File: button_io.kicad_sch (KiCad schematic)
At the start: 0 parts

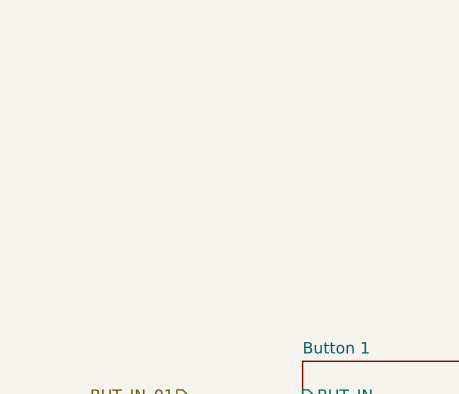
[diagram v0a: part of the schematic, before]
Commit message: Labeled expansion port, fixed en pin U19 (high)
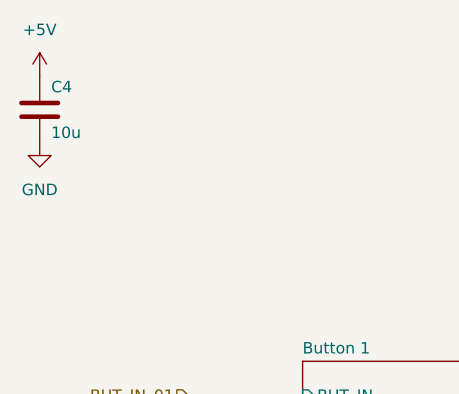
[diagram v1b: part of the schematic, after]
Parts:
- added C4: 10u, Capacitor_SMD:C_0805_2012Metric, symbol Device:C
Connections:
- new net +5V: C4.1
- new net GND: C4.2
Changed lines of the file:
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@@
+		)
+	)
+	(symbol
+		(lib_id "power:+5V")
+		(at 39.37 22.86 0)
+		(unit 1)
+		(exclude_from_sim no)
+		(in_bom yes)
+		(on_board yes)
+		(dnp no)
+		(fields_autoplaced yes)
+		(property "Reference" "#PWR052"
+			(at 39.37 26.67 0)
+			(effects
+				(font
+					(size 1.27 1.27)
+				)
+				(hide yes)
+			)
+		)
+		(property "Value" "+5V"
+			(at 39.37 17.78 0)
+			(effects
+				(font
+					(size 1.27 1.27)
+				)
+			)
+		)
+		(property "Footprint" ""
+			(at 39.37 22.86 0)
+			(effects
+				(font
+					(size 1.27 1.27)
+				)
+				(hide yes)
+			)
+		)
+		(property "Datasheet" ""
+			(at 39.37 22.86 0)
+			(effects
+				(font
+					(size 1.27 1.27)
+				)
+				(hide yes)
+			)
+		)
+		(property "Description" "Power symbol creates a global label with name \"+5V\""
+			(at 39.37 22.86 0)
+			(effects
+				(font
+					(size 1.27 1.27)
+				)
+				(hide yes)
+			)
+		)
+		(pin "1"
+		)
+		(instances
+			(project ""
+				(path "/4ab90003-ea4c-4878-8117-f834ac24f8d9/2279bf67-9a91-44f0-b5c7-36e7b6560aca"
+					(reference "#PWR052")
+					(unit 1)
+				)
+			)
+		)
+	)
+	(symbol
+		(lib_id "Device:C")
+		(at 39.37 26.67 0)
+		(unit 1)
+		(exclude_from_sim no)
+		(in_bom yes)
+		(on_board yes)
+		(dnp no)
+		(property "Reference" "C4"
+			(at 40.64 24.13 0)
+			(effects
+				(font
+					(size 1.27 1.27)
+				)
+				(justify left)
+			)
+		)
+		(property "Value" "10u"
+			(at 40.64 29.21 0)
+			(effects
+				(font
+					(size 1.27 1.27)
+				)
+				(justify left)
+			)
+		)
+		(property "Footprint" "Capacitor_SMD:C_0805_2012Metric"
+			(at 40.3352 30.48 0)
+			(effects
+				(font
+					(size 1.27 1.27)
+				)
+				(hide yes)
+			)
+		)
+		(property "Datasheet" "https://www.lcsc.com/product-detail/Multilayer-Ceramic-Capacitors-MLCC-SMD-SMT_Samsung-Electro-Mechanics-CL21B106KAYQNNE_C3039694.html"
+			(at 39.37 26.67 0)
+			(effects
+				(font
+					(size 1.27 1.27)
+				)
+				(hide yes)
+			)
+		)
+		(property "Description" ""
+			(at 39.37 26.67 0)
+			(effects
+				(font
+					(size 1.27 1.27)
+				)
+				(hide yes)
+			)
+		)
+		(property "LCSC" "C3039694"
+			(at 39.37 26.67 0)
+			(effects
+				(font
+					(size 1.27 1.27)
+				)
+				(hide yes)
+			)
+		)
+		(property "Check_prices" ""
+			(at 39.37 26.67 0)
+			(effects
+				(font
+					(size 1.27 1.27)
+				)
+				(hide yes)
+			)
+		)
+		(property "Description_1" ""
+			(at 39.37 26.67 0)
+			(effects
+				(font
+					(size 1.27 1.27)
+				)
+				(hide yes)
+			)
+		)
+		(property "Category" ""
+			(at 39.37 26.67 0)
+			(effects
+				(font
+					(size 1.27 1.27)
+				)
+				(hide yes)
+			)
+		)
+		(pin "1"
+		)
+		(pin "2"
+		)
+		(instances
+			(project "stopnu-hardware"
+				(path "/4ab90003-ea4c-4878-8117-f834ac24f8d9/2279bf67-9a91-44f0-b5c7-36e7b6560aca"
+					(reference "C4")
+					(unit 1)
+				)
+			)
+		)
+	)
+	(symbol
+		(lib_id "power:GND")
+		(at 39.37 30.48 0)
+		(unit 1)
+		(exclude_from_sim no)
+		(in_bom yes)
+		(on_board yes)
+		(dnp no)
+		(fields_autoplaced yes)
+		(property "Reference" "#PWR051"
+			(at 39.37 36.83 0)
+			(effects
+				(font
+					(size 1.27 1.27)
+				)
+				(hide yes)
+			)
+		)
+		(property "Value" "GND"
+			(at 39.37 35.56 0)
+			(effects
+				(font
+					(size 1.27 1.27)
+				)
+			)
+		)
+		(property "Footprint" ""
+			(at 39.37 30.48 0)
+			(effects
+				(font
+					(size 1.27 1.27)
+				)
+				(hide yes)
+			)
+		)
+		(property "Datasheet" ""
+			(at 39.37 30.48 0)
+			(effects
+				(font
+					(size 1.27 1.27)
+				)
+				(hide yes)
+			)
+		)
+		(property "Description" "Power symbol creates a global label with name \"GND\" , ground"
+			(at 39.37 30.48 0)
+			(effects
+				(font
+					(size 1.27 1.27)
+				)
+				(hide yes)
+			)
+		)
+		(pin "1"
+		)
+		(instances
+			(project ""
+				(path "/4ab90003-ea4c-4878-8117-f834ac24f8d9/2279bf67-9a91-44f0-b5c7-36e7b6560aca"
+					(reference "#PWR051")
+					(unit 1)
+				)
+			)
 		)
 	)
